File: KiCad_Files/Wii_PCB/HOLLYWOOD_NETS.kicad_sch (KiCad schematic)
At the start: 27 parts

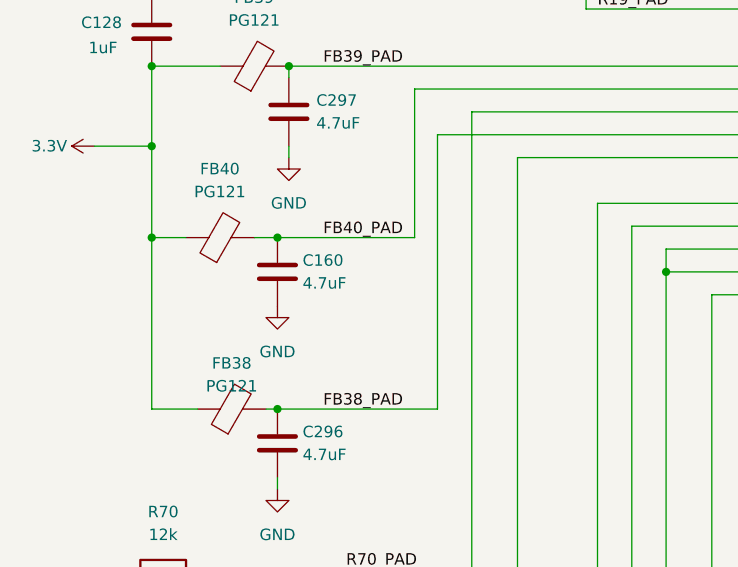
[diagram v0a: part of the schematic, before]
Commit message: Corrected C160 & RAM ZQ
C160 was updated from 4.7uF to 100nF.
RAM ZQ was grounded, it was working while floating, but updating anyway to ensure proper function.
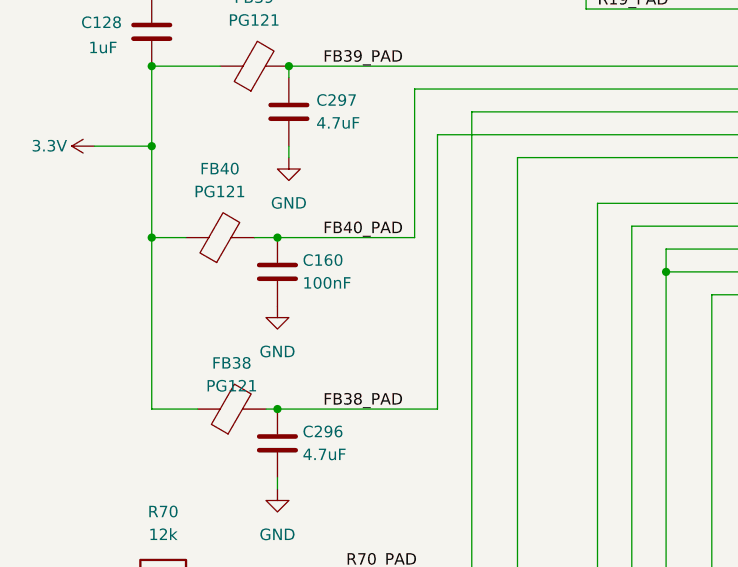
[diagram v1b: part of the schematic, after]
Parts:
- C160: value 4.7uF -> 100nF
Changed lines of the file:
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@@
 			)
 		)
-		(property "Value" "4.7uF"
+		(property "Value" "100nF"
 			(at 73.914 82.55 0)
 			(effects

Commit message: Updated RAM & GPU bus to allow custom net rules for measuring intra-track spacing, added pad for reset, removed debug pads, reorganized ram schematic to cluster length matched signals, changed MX chip and U10 symbols, and re-labeled the wifi net interface.
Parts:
- HOLLYWOOD1: footprint wii_bgaLibrary:Updated HOLLYWOOD -> WeeWii_Library:Updated HOLLYWOOD
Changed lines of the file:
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@@
 			)
 		)
-		(property "Footprint" "wii_bgaLibrary:Updated HOLLYWOOD"
+		(property "Footprint" "WeeWii_Library:Updated HOLLYWOOD"
 			(at 148.59 36.576 0)
 			(effects
@@
 		(pin "AD19"
 		)
-		(pin ""
+		(pin "D19"
 		)
 		(pin "A6"
@@
 		(pin "B3"
 		)
-		(pin ""
+		(pin "B14"
 		)
 		(pin "A5"
@@
 		(pin "C16"
 		)
+		(pin "E14"
+		)
+		(pin "D22"
+		)
+		(pin "B20"
+		)
+		(pin "C20"
+		)
+		(pin "C10"
+		)
+		(pin "C19"
+		)
+		(pin "E13"
+		)
+		(pin "D21"
+		)
+		(pin "D20"
+		)
+		(pin "D13"
+		)
+		(pin "R25"
+		)
+		(pin "A19"
+		)
+		(pin "D11"
+		)
+		(pin "B15"
+		)
+		(pin "D27"
+		)
+		(pin "D14"
+		)
+		(pin "D23"
+		)
+		(pin "C7"
+		)
+		(pin "E24"
+		)
+		(pin "B9"
+		)
+		(pin "A23"
+		)
+		(pin "D8"
+		)
+		(pin "D28"
+		)
+		(pin "A18"
+		)
+		(pin "E17"
+		)
+		(pin "B23"
+		)
+		(pin "C11"
+		)
+		(pin "A14"
+		)
+		(pin "C14"
+		)
+		(pin "H10"
+		)
+		(pin "C15"
+		)
 		(pin "D16"
 		)
-		(pin "D22"
-		)
-		(pin "B20"
-		)
-		(pin "C20"
-		)
-		(pin "C10"
-		)
-		(pin "C19"
-		)
-		(pin "E13"
-		)
-		(pin "D21"
-		)
-		(pin "D20"
-		)
-		(pin "D13"
-		)
-		(pin "R25"
-		)
-		(pin "A19"
-		)
-		(pin "D11"
-		)
-		(pin "B15"
-		)
-		(pin "D27"
-		)
-		(pin "D14"
-		)
-		(pin "D23"
-		)
-		(pin "C7"
-		)
-		(pin "E24"
-		)
-		(pin "B9"
-		)
-		(pin "A23"
-		)
-		(pin "D8"
-		)
-		(pin "D28"
-		)
-		(pin "A18"
-		)
-		(pin "E17"
-		)
-		(pin "B23"
-		)
-		(pin "C11"
-		)
-		(pin "A14"
-		)
-		(pin "C14"
-		)
-		(pin "H10"
-		)
-		(pin "C15"
-		)
-		(pin "D16"
-		)
 		(pin "G26"
 		)
@@
 		(pin "AG6"
 		)
+		(pin "A24"
+		)
+		(pin "N10"
+		)
 		(instances
